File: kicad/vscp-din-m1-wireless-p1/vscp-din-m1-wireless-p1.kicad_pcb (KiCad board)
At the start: 2 copper layers, 67 x 50 mm, 31 parts, among them J1 Conn_01x04_Left, J2 Conn_01x04_Right, J3 Conn_01x06, Q1 BC547, U1 ESP32-WROOM-32D, U2 ESP-12E

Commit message: Generated gerbers
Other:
- board text added: "DIN Wireles Controller M1"
- board text added: "Grodans Paradis AB https://www.grodansparadis.com https://www.vscp.org"

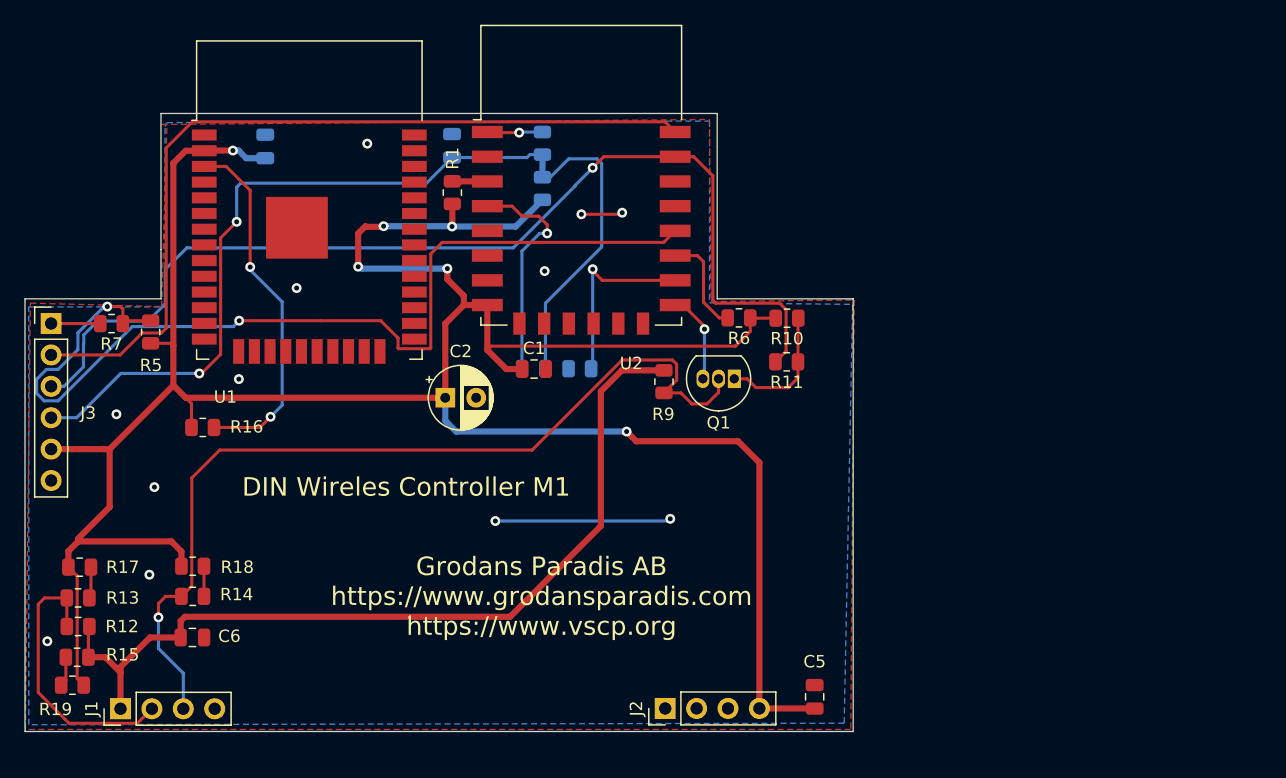
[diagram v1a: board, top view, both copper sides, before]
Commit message: Added vanilla DIN board
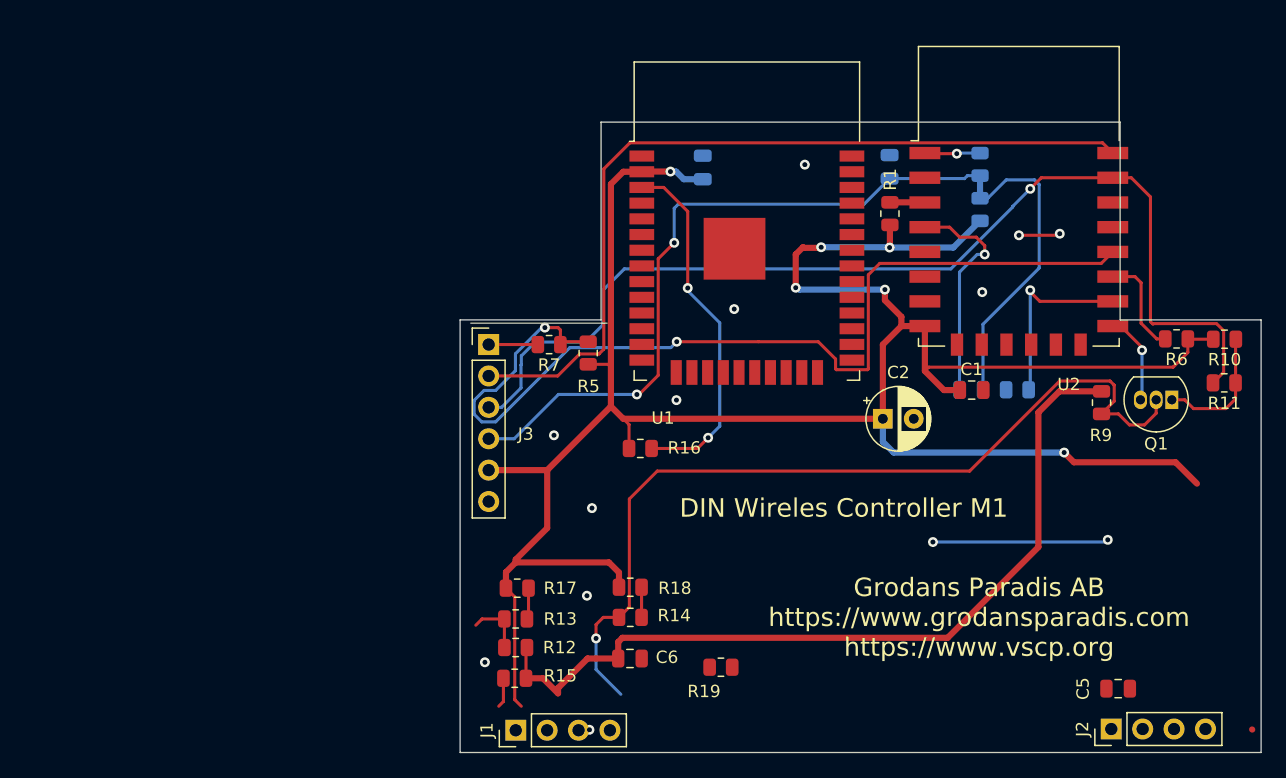
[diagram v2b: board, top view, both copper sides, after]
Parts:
- moved R19 52.5 mm to (126.3, 114.8)
- moved J2 36.1 mm to (157.9, 119.8)
- moved C1 35.4 mm to (146.6, 92.4)
- moved C2 35.4 mm to (139.4, 94.7)
- moved C3 35.4 mm to (139.9, 74.3)
- moved C6 35.4 mm to (118.9, 114.1)
- moved Q1 35.4 mm to (162.8, 93.2)
- moved R1 35.4 mm to (140.0, 78.1)
- moved R10 35.4 mm to (167.0, 88.3)
- moved R13 35.4 mm to (109.7, 110.9)
- moved R15 35.4 mm to (109.6, 115.7)
- moved R16 35.4 mm to (119.8, 97.1)
- moved R17 35.4 mm to (109.8, 108.4)
- moved R7 35.4 mm to (112.4, 88.7)
- moved U1 35.4 mm to (128.4, 81.7)
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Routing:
- net VCC: track 222.6 -> 198.2 mm
- net Net-(J1-Pad2): track 22.7 -> 4.83 mm, vias 1 -> 0
- net VDD: track 70.1 -> 67.1 mm
- net Net-(J1-Pad3): track 73.7 -> 70.8 mm
- net GND: vias 13 -> 14
- removed copper zone on B.Cu, net GND
- removed copper zone on F.Cu, net GND
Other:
- board size 67 x 50 mm -> 64.8 x 51 mm
